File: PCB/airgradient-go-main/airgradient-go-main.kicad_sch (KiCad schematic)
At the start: 204 parts, among them CN1 HCZZ0032-5, CN2 HCZZ0032-5, CN3 HCZZ0032-5, Q1 SIA445EDJ-T1-GE3, Q2 ZVN4106FTA_C508255, Q3 CSD83325L, Q4 SS8050-G, Q5 SI1308EDL, SW1 TS-1091C-A1B3-D2, SW2 TS-1091C-A1B3-D2, U1 W25N512GVEIG, U10 SGP41-D-R4, U11 PS1-CO-SMOKE-10k, U12 SHT4x, U13 SPL07-003, U14 LIS2DH12TR, U15 TMUX121NKGR_C22428404, U16 S12, U17 TCA6408ARGT, U18 TAU1113, U19 LM66200DRLR, U2 ZDSD512MLGEAG, U20 LP5036, U3 BQ27742YZFR-G1, U4 ESP32-C5-MINI-1, U5 BQ25628RYKR, U6 HYG-8503A, U7 TPL5010DDCR, U8 TPS63802DLAR, U9 TPS7A0228DQNR, Y1 32.768kHz CL6pF

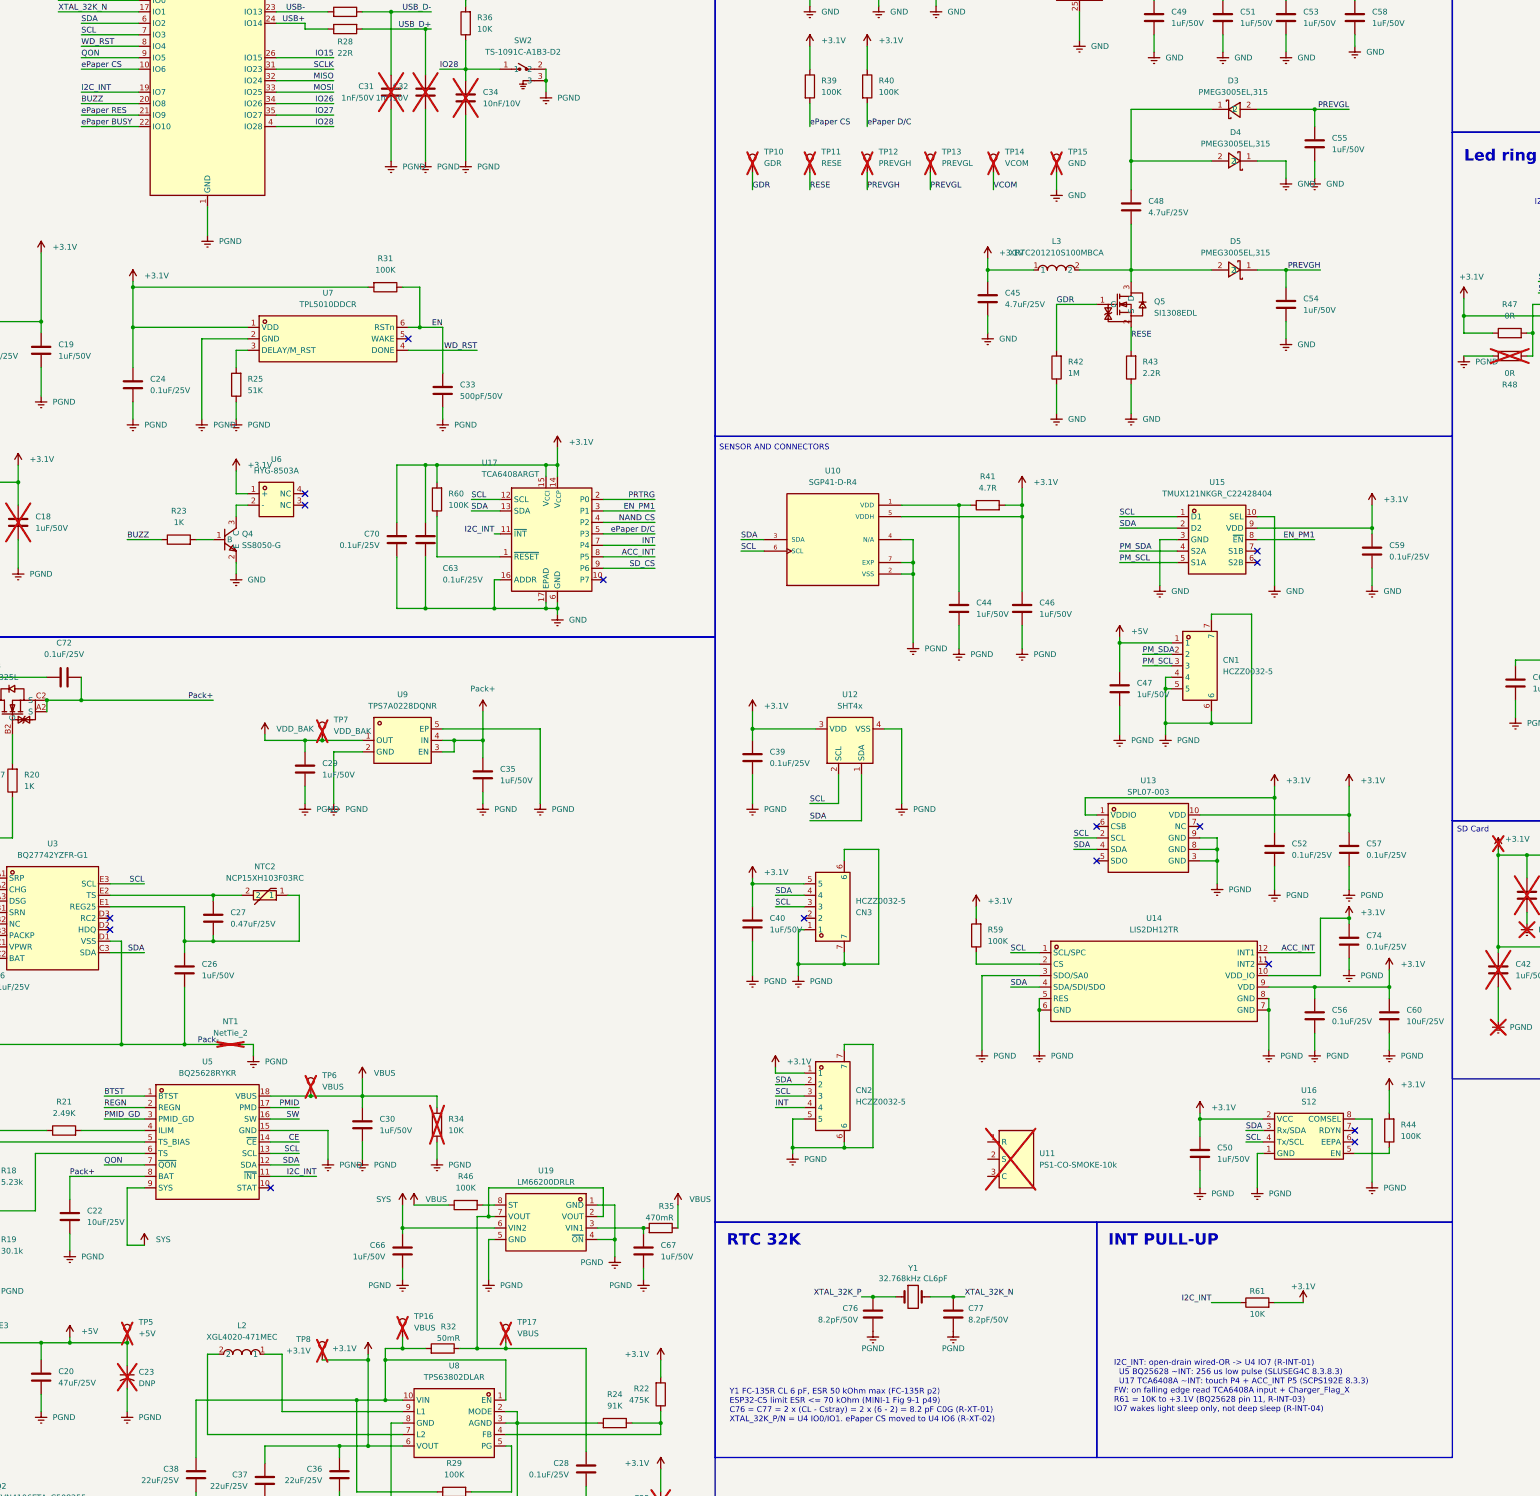
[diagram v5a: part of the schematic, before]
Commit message: Wire only the expander INT to IO7; charger INT stays NC
U5 pin 11 cannot leave the charger without re-doing its I2C escape:
it is boxed in by pad 12 SDA and its escape via, pad 10 STAT, L1's SYS
pad and the SYS pour on F.Cu, and the SW island on In2 under U5.

- EXP_INT: U17 TCA6408A ~INT -> U4 IO7. Touch (P4) and ACC_INT (P5)
  stop being polled.
- No external pull-up (R61 dropped): GPIO7's internal pull-up is
  enough because the TCA6408A holds INT low until its input port is
  read (SCPS192E 8.3.3).
- U5 ~INT keeps its NC flag; firmware reads the latched
  Charger_Flag_X registers instead (SLUSEG4C 8.3.8.1).
- INT LINE block is now notes only (R-INT-01..04).

lint: no new findings; ERC 269 -> 267 vs 1d977c7; net_diff 0 errors.
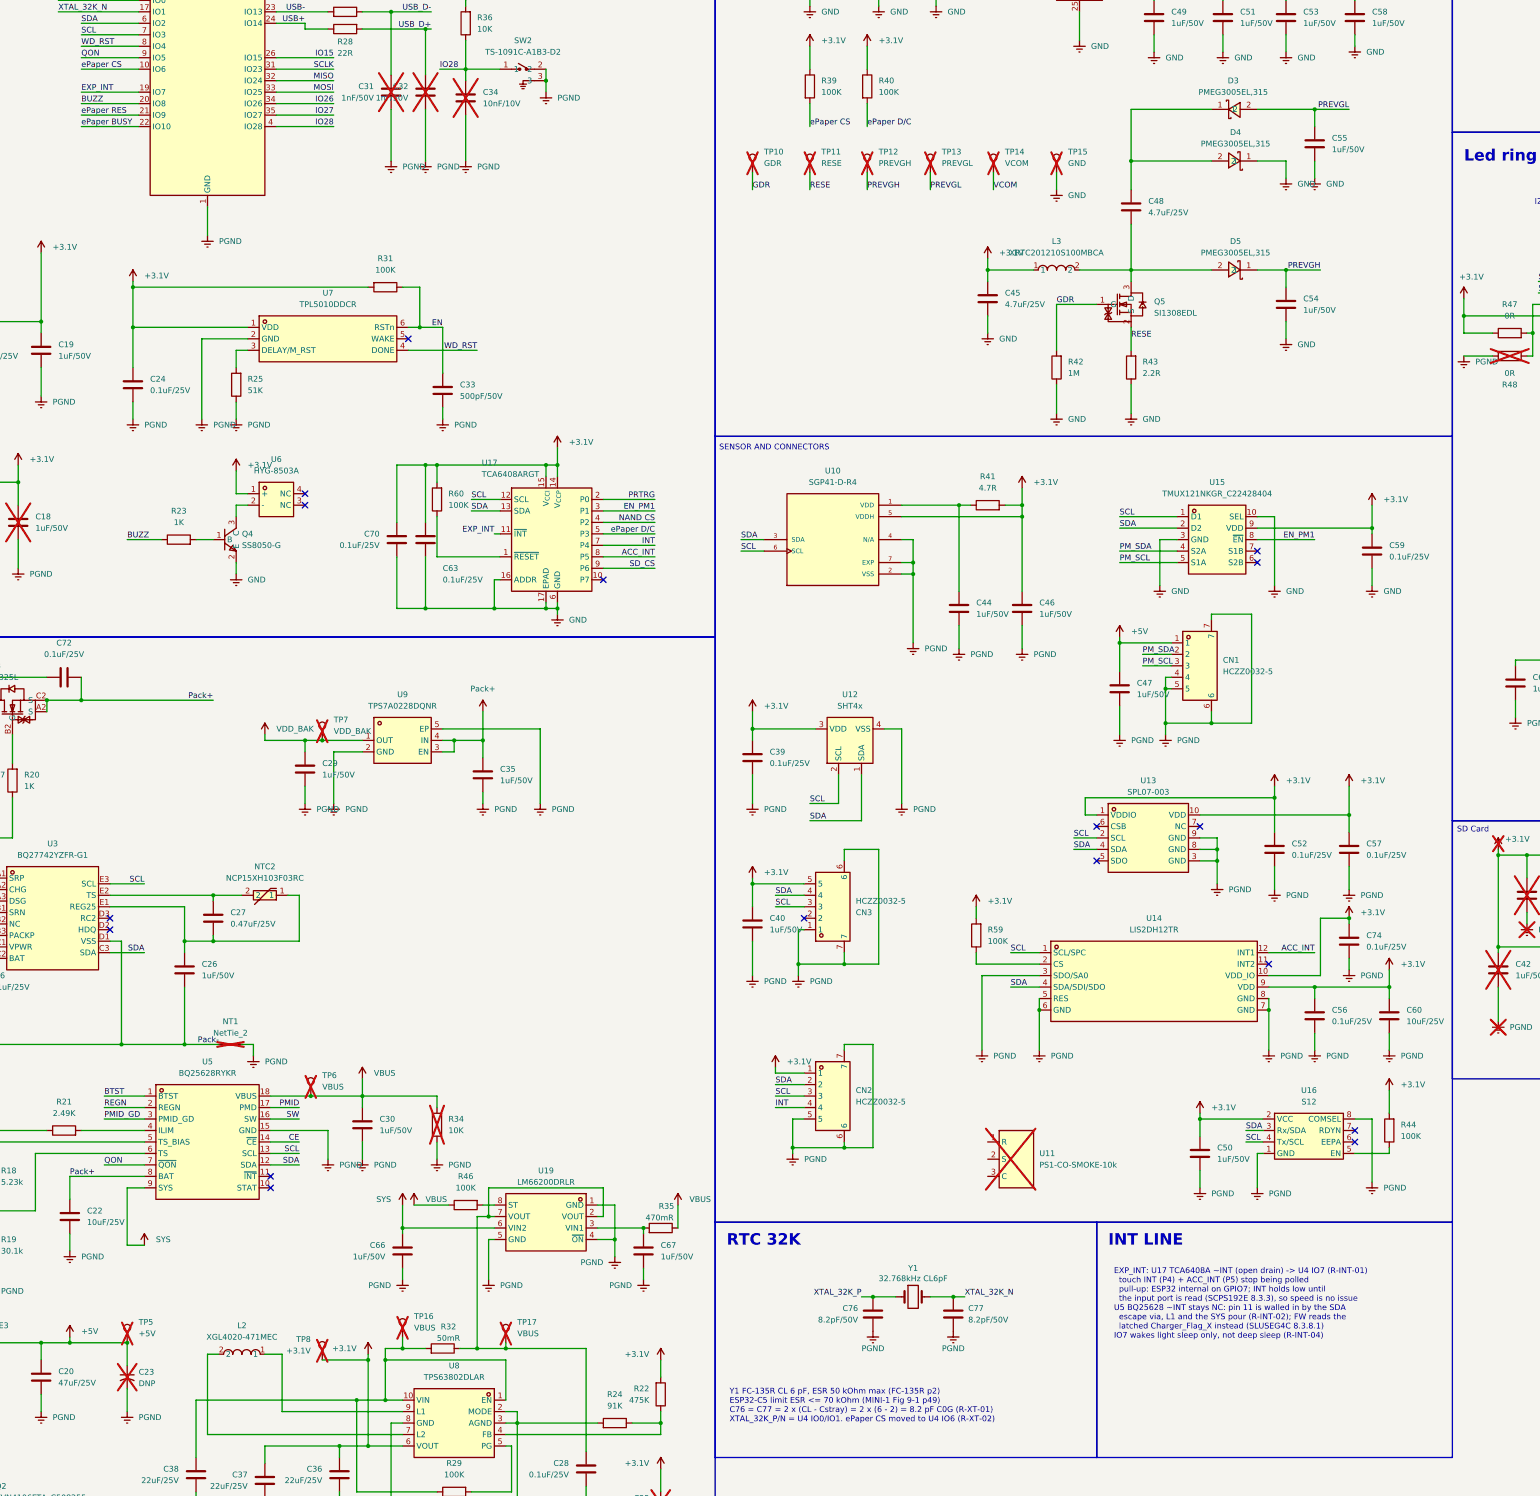
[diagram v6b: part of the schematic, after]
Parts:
- removed R61: 10K, Resistor_SMD:R_0402_1005Metric, symbol Device:R
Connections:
- net I2C_INT renamed EXP_INT
- net EXP_INT: no longer U5.11 (~{INT})
- no-connect marks 29 -> 30
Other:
- note added: "EXP_INT: U17 TCA6408A ~INT (open drain) -> U4 IO7 (R-INT-01) touch INT (P4) + ACC_INT (P5) stop being polled pull-up: ESP32 internal on GPIO7; INT holds low until the input port is read (SCPS192E 8.3.3), so speed is no issue U5 BQ25628 ~INT stays NC: pin 11 is walled in by the SDA escape via, L1 and the SYS pour (R-INT-02); FW reads the latched Charger_Flag_X instead (SLUSEG4C 8.3.8.1) IO7 wakes 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"
- note added: "INT LINE"
- note removed: "I2C_INT: open-drain wired-OR -> U4 IO7 (R-INT-01) U5 BQ25628 ~INT: 256 us low pulse (SLUSEG4C 8.3.8.3) U17 TCA6408A ~INT: touch P4 + ACC_INT P5 (SCPS192E 8.3.3) FW: on falling edge read TCA6408A input + Charger_Flag_X R61 = 10K to +3.1V (BQ25628 pin 11, R-INT-03) IO7 wakes light sleep only, not deep sleep (R-INT-04)"
- note removed: "INT PULL-UP"
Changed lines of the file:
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@@
 	)
 	(no_connect
+		(at 162.56 323.85)
+	)
+	(no_connect
 		(at 162.56 326.39)
 	)
@@
 	(wire
 		(pts
-			(xy 162.56 323.85) (xy 172.72 323.85)
-		)
-		(stroke
-			(width 0)
-			(type default)
-		)
-	)
-	(label "I2C_INT"
-		(at 172.72 323.85 180)
-		(effects
-			(font
-				(size 1.27 1.27)
-			)
-			(justify right bottom)
-		)
-	)
-	(wire
-		(pts
 			(xy 213.36 181.61) (xy 212.09 181.61)
 		)
@@
 		)
 	)
-	(label "I2C_INT"
+	(label "EXP_INT"
 		(at 212.09 181.61 180)
 		(effects
@@
 		)
 	)
-	(label "I2C_INT"
+	(label "EXP_INT"
 		(at 120.65 83.82 0)
 		(effects
@@
 		)
 	)
-	(wire
-		(pts
-			(xy 377.19 351.79) (xy 370.84 351.79)
-		)
-		(stroke
-			(width 0)
-			(type default)
-		)
-	)
-	(label "I2C_INT"
-		(at 370.84 351.79 180)
-		(effects
-			(font
-				(size 1.27 1.27)
-			)
-			(justify right bottom)
-		)
-	)
-	(wire
-		(pts
-			(xy 384.81 351.79) (xy 391.16 351.79)
-		)
-		(stroke
-			(width 0)
-			(type default)
-		)
-	)
-	(symbol
-		(lib_id "Device:R")
-		(at 381 351.79 90)
-		(unit 1)
-		(body_style 1)
-		(exclude_from_sim no)
-		(in_bom yes)
-		(on_board yes)
-		(in_pos_files yes)
-		(dnp no)
-		(fields_autoplaced yes)
-		(property "Reference" "R61"
-			(at 381 349.25 90)
-			(show_name no)
-			(do_not_autoplace no)
-			(effects
-				(font
-					(size 1.27 1.27)
-				)
-			)
-		)
-		(property "Value" "10K"
-			(at 381 354.33 90)
-			(show_name no)
-			(do_not_autoplace no)
-			(effects
-				(font
-					(size 1.27 1.27)
-				)
-			)
-		)
-		(property "Footprint" "Resistor_SMD:R_0402_1005Metric"
-			(at 381 351.79 0)
-			(hide yes)
-			(show_name no)
-			(do_not_autoplace no)
-			(effects
-				(font
-					(size 1.27 1.27)
-				)
-			)
-		)
-		(property "Datasheet" "https://lcsc.com/product-detail/Others_Huaxin-S-T-MR04X1002FTL_C327797.html"
-			(at 381 351.79 0)
-			(hide yes)
-			(show_name no)
-			(do_not_autoplace no)
-			(effects
-				(font
-					(size 1.27 1.27)
-				)
-			)
-		)
-		(property "Description" "MR04X1002FTL"
-			(at 381 351.79 0)
-			(hide yes)
-			(show_name no)
-			(do_not_autoplace no)
-			(effects
-				(font
-					(size 1.27 1.27)
-				)
-			)
-		)
-		(property "LCSC Part" "C327797"
-			(at 381 351.79 0)
-			(hide yes)
-			(show_name no)
-			(do_not_autoplace no)
-			(effects
-				(font
-					(size 1.27 1.27)
-				)
-			)
-		)
-		(pin "1"
-		)
-		(pin "2"
-		)
-		(instances
-			(project "airgradient-go-main"
-				(path "/63bfc1c7-4623-455a-8f83-dca1d491c7db"
-					(reference "R61")
-					(unit 1)
-				)
-			)
-		)
-	)
-	(symbol
-		(lib_id "power:VDD")
-		(at 391.16 351.79 0)
-		(unit 1)
-		(body_style 1)
-		(exclude_from_sim no)
-		(in_bom yes)
-		(on_board yes)
-		(in_pos_files yes)
-		(dnp no)
-		(fields_autoplaced yes)
-		(property "Reference" "#PWR003"
-			(at 391.16 355.6 0)
-			(hide yes)
-			(show_name no)
-			(do_not_autoplace no)
-			(effects
-				(font
-					(size 1.27 1.27)
-				)
-			)
-		)
-		(property "Value" "+3.1V"
-			(at 391.16 348.234 0)
-			(show_name no)
-			(do_not_autoplace no)
-			(effects
-				(font
-					(size 1.27 1.27)
-				)
-			)
-		)
-		(property "Footprint" ""
-			(at 391.16 351.79 0)
-			(hide yes)
-			(show_name no)
-			(do_not_autoplace no)
-			(effects
-				(font
-					(size 1.27 1.27)
-				)
-			)
-		)
-		(property "Datasheet" ""
-			(at 391.16 351.79 0)
-			(hide yes)
-			(show_name no)
-			(do_not_autoplace no)
-			(effects
-				(font
-					(size 1.27 1.27)
-				)
-			)
-		)
-		(property "Description" "Power symbol creates a global label with name \"VDD\""
-			(at 391.16 351.79 0)
-			(hide yes)
-			(show_name no)
-			(do_not_autoplace no)
-			(effects
-				(font
-					(size 1.27 1.27)
-				)
-			)
-		)
-		(pin "1"
-		)
-		(instances
-			(project "airgradient-go-main"
-				(path "/63bfc1c7-4623-455a-8f83-dca1d491c7db"
-					(reference "#PWR003")
-					(unit 1)
-				)
-			)
-		)
-	)
 	(rectangle
 		(start 345.44 334.01)
@@
 		)
 	)
-	(text "INT PULL-UP"
+	(text "INT LINE"
 		(exclude_from_sim no)
 		(at 347.98 336.55 0)
@@
 		)
 	)
-	(text "I2C_INT: open-drain wired-OR -> U4 IO7 (R-INT-01)\n  U5 BQ25628 ~INT: 256 us low pulse (SLUSEG4C 8.3.8.3)\n  U17 TCA6408A ~INT: touch P4 + ACC_INT P5 (SCPS192E 8.3.3)\nFW: on falling edge read TCA6408A input + Charger_Flag_X\nR61 = 10K to +3.1V (BQ25628 pin 11, R-INT-03)\nIO7 wakes light sleep only, not deep sleep (R-INT-04)"
+	(text "EXP_INT: U17 TCA6408A ~INT (open drain) -> U4 IO7 (R-INT-01)\n  touch INT (P4) + ACC_INT (P5) stop being polled\n  pull-up: ESP32 internal on GPIO7; INT holds low until\n  the input port is read (SCPS192E 8.3.3), so speed is no issue\nU5 BQ25628 ~INT stays NC: pin 11 is walled in by the SDA\n  escape via, L1 and the SYS pour (R-INT-02); FW reads the\n  latched Charger_Flag_X instead (SLUSEG4C 8.3.8.1)\nIO7 wakes light sleep only, not deep sleep (R-INT-04)"
 		(exclude_from_sim no)
-		(at 349.25 364.49 0)
+		(at 349.25 344.17 0)
 		(effects
 			(font
